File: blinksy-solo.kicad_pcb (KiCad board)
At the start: 2 copper layers, 69.8 x 50.8 mm, 24 parts, among them P1 D1, P10 PWR, P2 D2, P3 D3, P4 D4, P5 D5, P6 D6, P7 D7, P8 D8, P9 AUX_DATA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

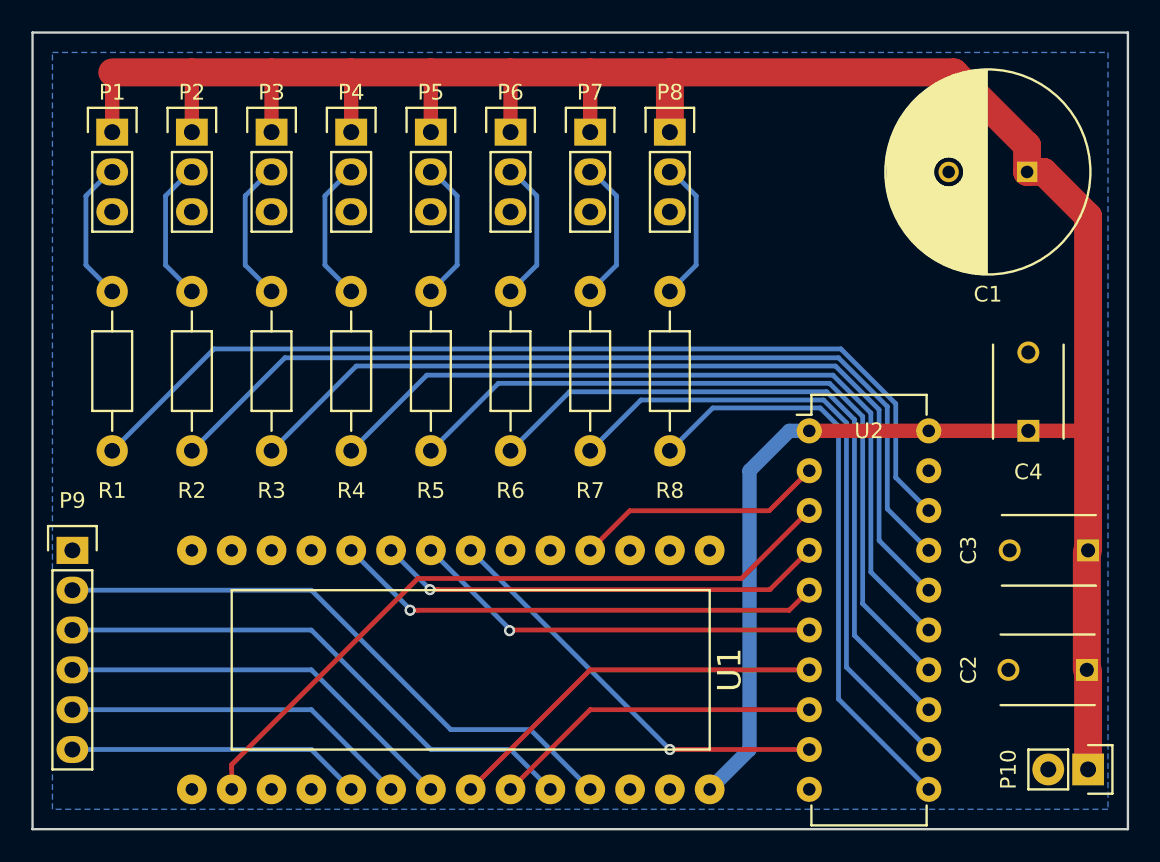
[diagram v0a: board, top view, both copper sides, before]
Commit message: redraw ground ground plane closer to edge
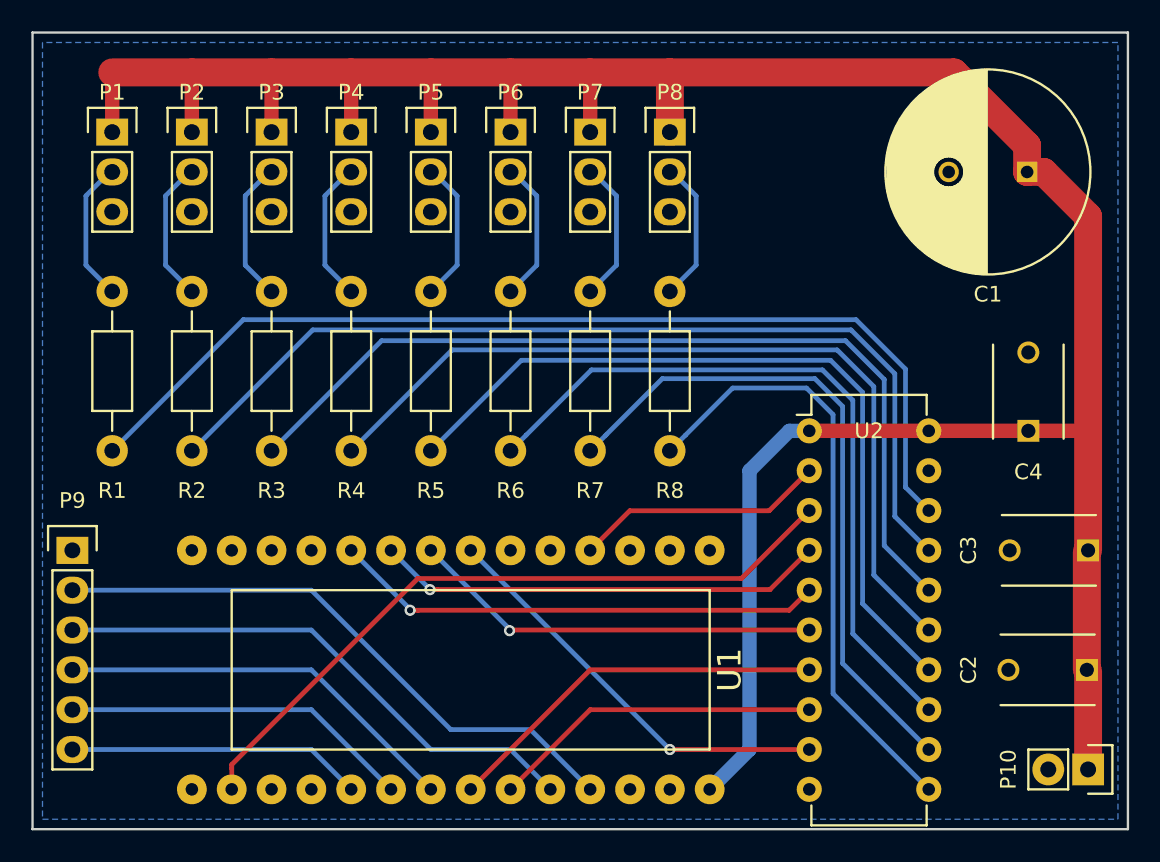
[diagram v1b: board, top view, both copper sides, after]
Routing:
- net Net-(R1-Pad1): track 61.8 -> 65.0 mm
- net Net-(R2-Pad1): track 58.4 -> 61.3 mm
- net Net-(R3-Pad1): track 55.0 -> 57.6 mm
- net Net-(R4-Pad1): track 51.5 -> 53.9 mm
- net Net-(R5-Pad1): track 48.1 -> 50.2 mm
- net Net-(R6-Pad1): track 44.7 -> 46.5 mm
- net Net-(R7-Pad1): track 41.3 -> 42.9 mm
- net Net-(R8-Pad1): track 37.9 -> 39.2 mm
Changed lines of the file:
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@@
   (general
     (links 61)
-    (no_connects 7)
+    (no_connects 1)
     (area 126.924999 76.124999 196.925001 127.075001)
     (thickness 1.6)
     (drawings 4)
-    (tracks 150)
+    (tracks 153)
     (zones 0)
     (modules 24)
@@
   (segment (start 129.54 121.92) (end 144.78 121.92) (width 0.3048) (layer B.Cu) (net 15))
   (segment (start 144.78 121.92) (end 147.32 124.46) (width 0.3048) (layer B.Cu) (net 15))
-  (segment (start 184.15 106.68) (end 182.04477 104.57477) (width 0.3048) (layer B.Cu) (net 16) (status 10))
-  (segment (start 182.04477 104.57477) (end 182.04477 99.872236) (width 0.3048) (layer B.Cu) (net 16))
-  (segment (start 182.04477 99.872236) (end 178.54793 96.375396) (width 0.3048) (layer B.Cu) (net 16))
-  (segment (start 178.54793 96.375396) (end 138.574604 96.375396) (width 0.3048) (layer B.Cu) (net 16))
-  (segment (start 138.574604 96.375396) (end 132.08 102.87) (width 0.3048) (layer B.Cu) (net 16) (status 20))
-  (segment (start 184.15 109.22) (end 181.506794 106.576794) (width 0.3048) (layer B.Cu) (net 17) (status 10))
-  (segment (start 181.506794 106.576794) (end 181.506794 100.052696) (width 0.3048) (layer B.Cu) (net 17))
-  (segment (start 181.506794 100.052696) (end 178.395783 96.941685) (width 0.3048) (layer B.Cu) (net 17))
-  (segment (start 178.395783 96.941685) (end 143.088315 96.941685) (width 0.3048) (layer B.Cu) (net 17))
-  (segment (start 143.088315 96.941685) (end 137.16 102.87) (width 0.3048) (layer B.Cu) (net 17) (status 20))
-  (segment (start 184.15 111.76) (end 180.982976 108.592976) (width 0.3048) (layer B.Cu) (net 18) (status 10))
-  (segment (start 180.982976 108.592976) (end 180.982976 100.247314) (width 0.3048) (layer B.Cu) (net 18))
-  (segment (start 180.982976 100.247314) (end 178.201165 97.465503) (width 0.3048) (layer B.Cu) (net 18))
-  (segment (start 178.201165 97.465503) (end 147.644497 97.465503) (width 0.3048) (layer B.Cu) (net 18))
-  (segment (start 147.644497 97.465503) (end 142.24 102.87) (width 0.3048) (layer B.Cu) (net 18) (status 20))
-  (segment (start 184.15 114.3) (end 180.459158 110.609158) (width 0.3048) (layer B.Cu) (net 19) (status 10))
-  (segment (start 180.459158 110.609158) (end 180.459158 100.466839) (width 0.3048) (layer B.Cu) (net 19))
-  (segment (start 180.459158 100.466839) (end 178.038269 98.04595) (width 0.3048) (layer B.Cu) (net 19))
-  (segment (start 178.038269 98.04595) (end 152.14405 98.04595) (width 0.3048) (layer B.Cu) (net 19))
-  (segment (start 152.14405 98.04595) (end 147.32 102.87) (width 0.3048) (layer B.Cu) (net 19) (status 20))
-  (segment (start 184.15 116.84) (end 179.93534 112.62534) (width 0.3048) (layer B.Cu) (net 20) (status 10))
-  (segment (start 177.825912 98.569769) (end 156.700231 98.569769) (width 0.3048) (layer B.Cu) (net 20))
-  (segment (start 179.93534 112.62534) (end 179.93534 100.679197) (width 0.3048) (layer B.Cu) (net 20))
-  (segment (start 156.700231 98.569769) (end 152.4 102.87) (width 0.3048) (layer B.Cu) (net 20) (status 20))
-  (segment (start 179.93534 100.679197) (end 177.825912 98.569769) (width 0.3048) (layer B.Cu) (net 20))
-  (segment (start 184.15 119.38) (end 179.409871 114.639871) (width 0.3048) (layer B.Cu) (net 21) (status 10))
-  (segment (start 179.409871 114.639871) (end 179.409871 100.879331) (width 0.3048) (layer B.Cu) (net 21))
-  (segment (start 179.409871 100.879331) (end 177.638284 99.107744) (width 0.3048) (layer B.Cu) (net 21))
-  (segment (start 177.638284 99.107744) (end 161.242256 99.107744) (width 0.3048) (layer B.Cu) (net 21))
-  (segment (start 161.242256 99.107744) (end 157.48 102.87) (width 0.3048) (layer B.Cu) (net 21) (status 20))
-  (segment (start 184.15 121.92) (end 178.901861 116.671861) (width 0.3048) (layer B.Cu) (net 22) (status 10))
-  (segment (start 178.901861 116.671861) (end 178.901861 101.089757) (width 0.3048) (layer B.Cu) (net 22))
-  (segment (start 165.798438 99.631562) (end 162.56 102.87) (width 0.3048) (layer B.Cu) (net 22) (status 20))
-  (segment (start 178.901861 101.089757) (end 177.443666 99.631562) (width 0.3048) (layer B.Cu) (net 22))
-  (segment (start 177.443666 99.631562) (end 165.798438 99.631562) (width 0.3048) (layer B.Cu) (net 22))
-  (segment (start 170.3704 100.1396) (end 167.64 102.87) (width 0.3048) (layer B.Cu) (net 23) (status 20))
-  (segment (start 177.230993 100.139599) (end 170.3704 100.1396) (width 0.3048) (layer B.Cu) (net 23))
-  (segment (start 178.39385 118.70385) (end 178.39385 101.302458) (width 0.3048) (layer B.Cu) (net 23))
-  (segment (start 184.15 124.46) (end 178.39385 118.70385) (width 0.3048) (layer B.Cu) (net 23) (status 10))
-  (segment (start 178.39385 101.302458) (end 177.230993 100.139599) (width 0.3048) (layer B.Cu) (net 23))
+  (segment (start 184.15 106.68) (end 182.665861 105.195861) (width 0.3048) (layer B.Cu) (net 16))
+  (segment (start 182.665861 97.662101) (end 179.514376 94.510616) (width 0.3048) (layer B.Cu) (net 16))
+  (segment (start 182.665861 105.195861) (end 182.665861 97.662101) (width 0.3048) (layer B.Cu) (net 16))
+  (segment (start 179.514376 94.510616) (end 140.439384 94.510616) (width 0.3048) (layer B.Cu) (net 16))
+  (segment (start 140.439384 94.510616) (end 132.08 102.87) (width 0.3048) (layer B.Cu) (net 16))
+  (segment (start 184.15 109.22) (end 181.98589 107.05589) (width 0.3048) (layer B.Cu) (net 17))
+  (segment (start 181.98589 107.05589) (end 181.98589 97.95603) (width 0.3048) (layer B.Cu) (net 17))
+  (segment (start 181.98589 97.95603) (end 179.190554 95.160694) (width 0.3048) (layer B.Cu) (net 17))
+  (segment (start 179.190554 95.160694) (end 144.869306 95.160694) (width 0.3048) (layer B.Cu) (net 17))
+  (segment (start 144.869306 95.160694) (end 137.16 102.87) (width 0.3048) (layer B.Cu) (net 17))
+  (segment (start 184.15 111.76) (end 181.309808 108.919808) (width 0.3048) (layer B.Cu) (net 18))
+  (segment (start 181.309808 108.919808) (end 181.309808 98.320074) (width 0.3048) (layer B.Cu) (net 18))
+  (segment (start 181.309808 98.320074) (end 178.839511 95.849777) (width 0.3048) (layer B.Cu) (net 18))
+  (segment (start 178.839511 95.849777) (end 149.260223 95.849777) (width 0.3048) (layer B.Cu) (net 18))
+  (segment (start 149.260223 95.849777) (end 142.24 102.87) (width 0.3048) (layer B.Cu) (net 18))
+  (segment (start 184.15 114.3) (end 180.646729 110.796729) (width 0.3048) (layer B.Cu) (net 19))
+  (segment (start 180.646729 110.796729) (end 180.646729 98.777795) (width 0.3048) (layer B.Cu) (net 19))
+  (segment (start 180.646729 98.777795) (end 178.306447 96.437513) (width 0.3048) (layer B.Cu) (net 19))
+  (segment (start 178.306447 96.437513) (end 153.752487 96.437513) (width 0.3048) (layer B.Cu) (net 19))
+  (segment (start 153.752487 96.437513) (end 147.32 102.87) (width 0.3048) (layer B.Cu) (net 19))
+  (segment (start 184.15 116.84) (end 179.931643 112.621643) (width 0.3048) (layer B.Cu) (net 20))
+  (segment (start 179.931643 112.621643) (end 179.931643 99.141838) (width 0.3048) (layer B.Cu) (net 20))
+  (segment (start 179.931643 99.141838) (end 177.890397 97.100592) (width 0.3048) (layer B.Cu) (net 20))
+  (segment (start 177.890397 97.100592) (end 158.169408 97.100592) (width 0.3048) (layer B.Cu) (net 20))
+  (segment (start 158.169408 97.100592) (end 152.4 102.87) (width 0.3048) (layer B.Cu) (net 20))
+  (segment (start 184.15 119.38) (end 179.307567 114.537567) (width 0.3048) (layer B.Cu) (net 21))
+  (segment (start 179.307567 114.537567) (end 179.307567 99.648899) (width 0.3048) (layer B.Cu) (net 21))
+  (segment (start 179.307567 99.648899) (end 177.370334 97.711666) (width 0.3048) (layer B.Cu) (net 21))
+  (segment (start 177.370334 97.711666) (end 162.638334 97.711666) (width 0.3048) (layer B.Cu) (net 21))
+  (segment (start 162.638334 97.711666) (end 158.479489 101.870511) (width 0.3048) (layer B.Cu) (net 21))
+  (segment (start 158.479489 101.870511) (end 157.48 102.87) (width 0.3048) (layer B.Cu) (net 21))
+  (segment (start 184.15 121.92) (end 178.657489 116.427489) (width 0.3048) (layer B.Cu) (net 22))
+  (segment (start 176.889277 98.270733) (end 167.159267 98.270733) (width 0.3048) (layer B.Cu) (net 22))
+  (segment (start 178.657489 116.427489) (end 178.657489 100.038945) (width 0.3048) (layer B.Cu) (net 22))
+  (segment (start 178.657489 100.038945) (end 176.889277 98.270733) (width 0.3048) (layer B.Cu) (net 22))
+  (segment (start 167.159267 98.270733) (end 163.559489 101.870511) (width 0.3048) (layer B.Cu) (net 22))
+  (segment (start 163.559489 101.870511) (end 162.56 102.87) (width 0.3048) (layer B.Cu) (net 22))
+  (segment (start 184.15 124.46) (end 178.046416 118.356416) (width 0.3048) (layer B.Cu) (net 23))
+  (segment (start 178.046416 118.356416) (end 178.046416 100.559008) (width 0.3048) (layer B.Cu) (net 23))
+  (segment (start 178.046416 100.559008) (end 176.356213 98.868805) (width 0.3048) (layer B.Cu) (net 23))
+  (segment (start 176.356213 98.868805) (end 171.641195 98.868805) (width 0.3048) (layer B.Cu) (net 23))
+  (segment (start 171.641195 98.868805) (end 168.639489 101.870511) (width 0.3048) (layer B.Cu) (net 23))
+  (segment (start 168.639489 101.870511) (end 167.64 102.87) (width 0.3048) (layer B.Cu) (net 23))
   (segment (start 176.53 104.14) (end 173.977003 106.692997) (width 0.3048) (layer F.Cu) (net 26))
   (segment (start 173.977003 106.692997) (end 165.087003 106.692997) (width 0.3048) (layer F.Cu) (net 26))
@@
     (polygon
       (pts
-        (xy 128.27 77.47) (xy 195.58 77.47) (xy 195.58 125.73) (xy 128.27 125.73)
+        (xy 196.215 76.835) (xy 127.635 76.835) (xy 127.635 126.365) (xy 196.215 126.365)
       )
     )

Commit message: Expand ground plane more, fix disconnected pins
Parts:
- moved P10 2.54 mm to (191.8, 123.2)
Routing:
- net Net-(U1-Pad15): track 0.00 -> 2.54 mm
- net VCC: track 176.7 -> 179.3 mm
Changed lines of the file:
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@@
   (general
     (links 61)
-    (no_connects 1)
-    (area 126.924999 76.124999 196.925001 127.075001)
+    (no_connects 2)
+    (area 126.924999 76.124999 196.925001 127.483001)
     (thickness 1.6)
     (drawings 4)
-    (tracks 153)
+    (tracks 155)
     (zones 0)
     (modules 24)
@@
   )
   (module Pin_Headers:Pin_Header_Straight_1x02 (layer F.Cu)
-    (at 194.31 123.19 270)
+    (at 191.77 123.19 270)
     (descr "Through hole pin header")
     (tags "pin header")
@@
   (gr_line (start 127 127) (end 196.85 127) (layer Edge.Cuts) (width 0.15))
   (gr_line (start 127 76.2) (end 127 127) (layer Edge.Cuts) (width 0.15))
+  (segment (start 191.77 123.19) (end 194.31 123.19) (width 1.778) (layer F.Cu) (net 1))
   (segment (start 176.53 101.6) (end 175.26 101.6) (width 0.9144) (layer B.Cu) (net 1))
   (segment (start 175.26 101.6) (end 172.72 104.14) (width 0.9144) (layer B.Cu) (net 1))
@@
   (segment (start 139.7 122.884185) (end 139.7 123.116498) (width 0.3048) (layer F.Cu) (net 38))
   (segment (start 139.7 123.116498) (end 139.7 124.46) (width 0.3048) (layer F.Cu) (net 38))
+  (segment (start 142.24 124.46) (end 144.78 124.46) (width 0.3048) (layer B.Cu) (net 39))
   (segment (start 176.53 116.84) (end 162.56 116.84) (width 0.3048) (layer F.Cu) (net 40))
   (segment (start 162.56 116.84) (end 154.94 124.46) (width 0.3048) (layer F.Cu) (net 40))
@@
     (polygon
       (pts
-        (xy 196.215 76.835) (xy 127.635 76.835) (xy 127.635 126.365) (xy 196.215 126.365)
+        (xy 195.58 125.73) (xy 195.58 77.47) (xy 128.27 77.47) (xy 128.27 125.73)
       )
     )

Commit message: Minor layout touchups
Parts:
- moved C2 3.81 mm to (194.3, 113.0)
- moved C3 2.54 mm to (194.3, 106.7)
- moved C1 0.08 mm to (190.5, 85.1)
- moved C4 0.08 mm to (190.5, 101.5)
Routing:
- net /OCTO2: track 45.1 -> 46.8 mm
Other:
- net class Default: clearance 0.2032 -> 0.3048
- net class POWER: clearance 0.508 -> 0.3048
- rule trace_clearance: 0.2032 -> 0.3048
- board text added: "+"
- board text added: "-"
- board text added: "Blinksy Solo Rev1"

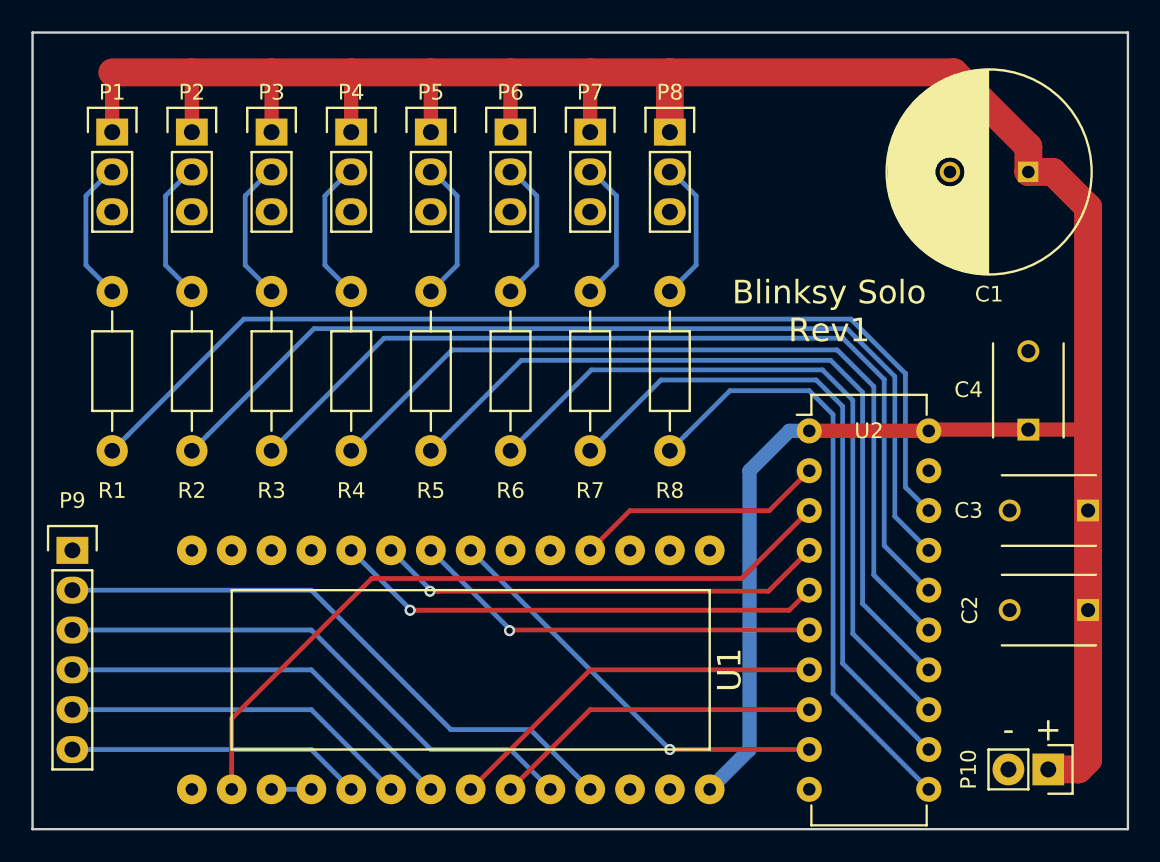
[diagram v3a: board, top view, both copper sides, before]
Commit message: Add footprint for 3mm screw holes
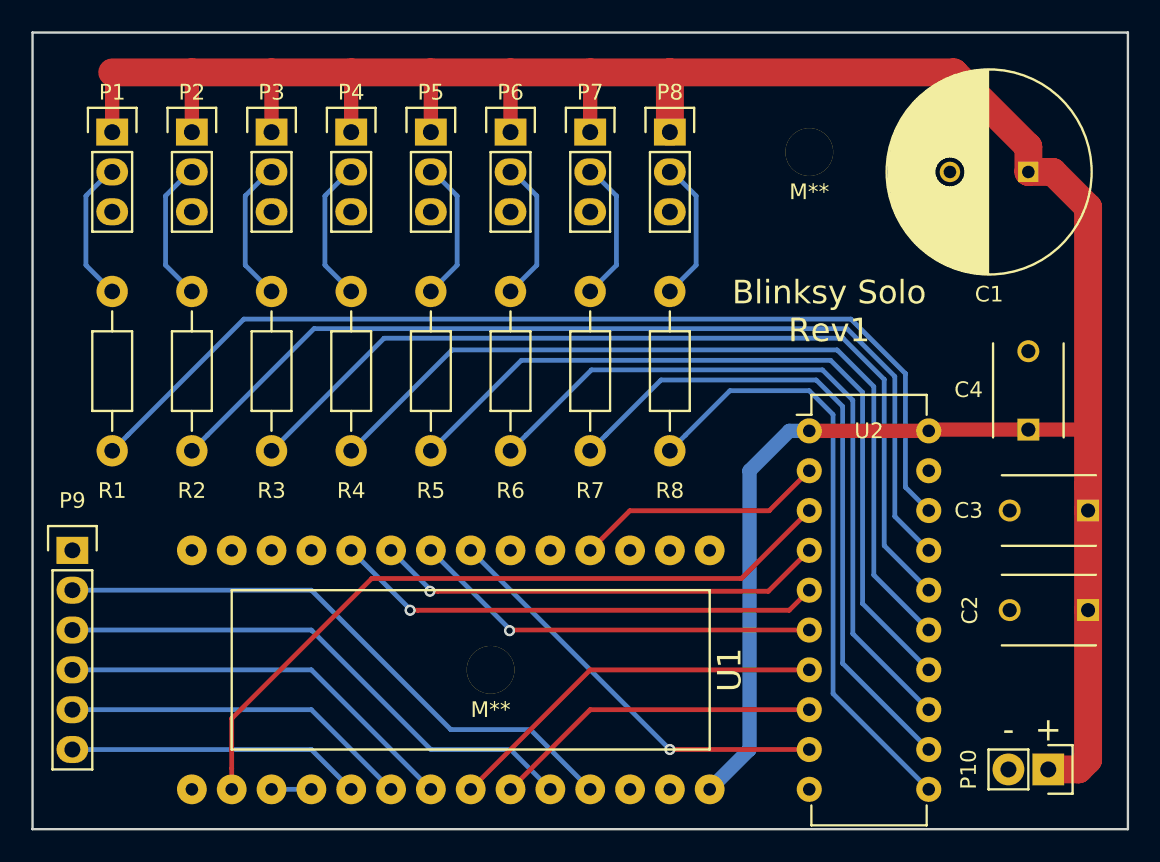
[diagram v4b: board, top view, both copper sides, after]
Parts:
- added M**: 3mm MNT, sinistral:3mmMNT, F.Cu at (156.2, 116.8)
- added M**: 3mm MNT, sinistral:3mmMNT, F.Cu at (176.5, 83.8)
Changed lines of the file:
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@@
   (general
     (links 61)
-    (no_connects 2)
-    (area 126.924999 76.124999 196.925001 127.483001)
+    (no_connects 0)
+    (area 126.924999 76.124999 196.925001 127.075001)
     (thickness 1.6)
     (drawings 7)
     (tracks 160)
     (zones 0)
-    (modules 24)
+    (modules 26)
     (nets 44)
   )
@@
     (visible_elements FFFFFF7F)
     (pcbplotparams
-      (layerselection 0x00030_80000001)
-      (usegerberextensions false)
+      (layerselection 0x010f0_80000001)
+      (usegerberextensions true)
       (excludeedgelayer true)
       (linewidth 0.100000)
@@
       (outputformat 1)
       (mirror false)
-      (drillshape 1)
+      (drillshape 0)
       (scaleselection 1)
-      (outputdirectory ""))
+      (outputdirectory gerber/blinksy-rev1/))
   )
   (net 0 "")
@@
     )
   )
+  (module sinistral:3mmMNT (layer F.Cu)
+    (at 156.21 116.84)
+    (fp_text reference M** (at 0 2.54) (layer F.SilkS)
+      (effects (font (size 1 1) (thickness 0.15)))
+    )
+    (fp_text value "3mm MNT" (at 0 -2.54) (layer F.Fab)
+      (effects (font (size 1 1) (thickness 0.15)))
+    )
+    (pad 1 thru_hole circle (at 0 0) (size 3.05 3.05) (drill 3.05) (layers *.Cu *.Mask F.SilkS))
+  )
+  (module sinistral:3mmMNT (layer F.Cu)
+    (at 176.53 83.82)
+    (fp_text reference M** (at 0 2.54) (layer F.SilkS)
+      (effects (font (size 1 1) (thickness 0.15)))
+    )
+    (fp_text value "3mm MNT" (at 0 -2.54) (layer F.Fab)
+      (effects (font (size 1 1) (thickness 0.15)))
+    )
+    (pad 1 thru_hole circle (at 0 0) (size 3.05 3.05) (drill 3.05) (layers *.Cu *.Mask F.SilkS))
+  )
   (gr_text - (at 189.23 120.65) (layer F.SilkS)
     (effects (font (size 1.5 1.5) (thickness 0.3)))
@@
     (effects (font (size 1.5 1.5) (thickness 0.3)))
   )
-  (gr_text "Blinksy Solo\nRev1" (at 177.8 93.98 360) (layer F.SilkS)
+  (gr_text "Blinksy Solo\nRev1" (at 177.8 93.98) (layer F.SilkS)
     (effects (font (size 1.5 1.5) (thickness 0.3)))
   )
